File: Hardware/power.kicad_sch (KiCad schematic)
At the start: 29 parts, among them IC1 LTC4413EDD#PBF, Q6 BUK9M11-40EX, Q8 DMP3099L, U3 LM66200DRLR, U4 MAX77827AEFD+T, U5 SC4215ASTRT

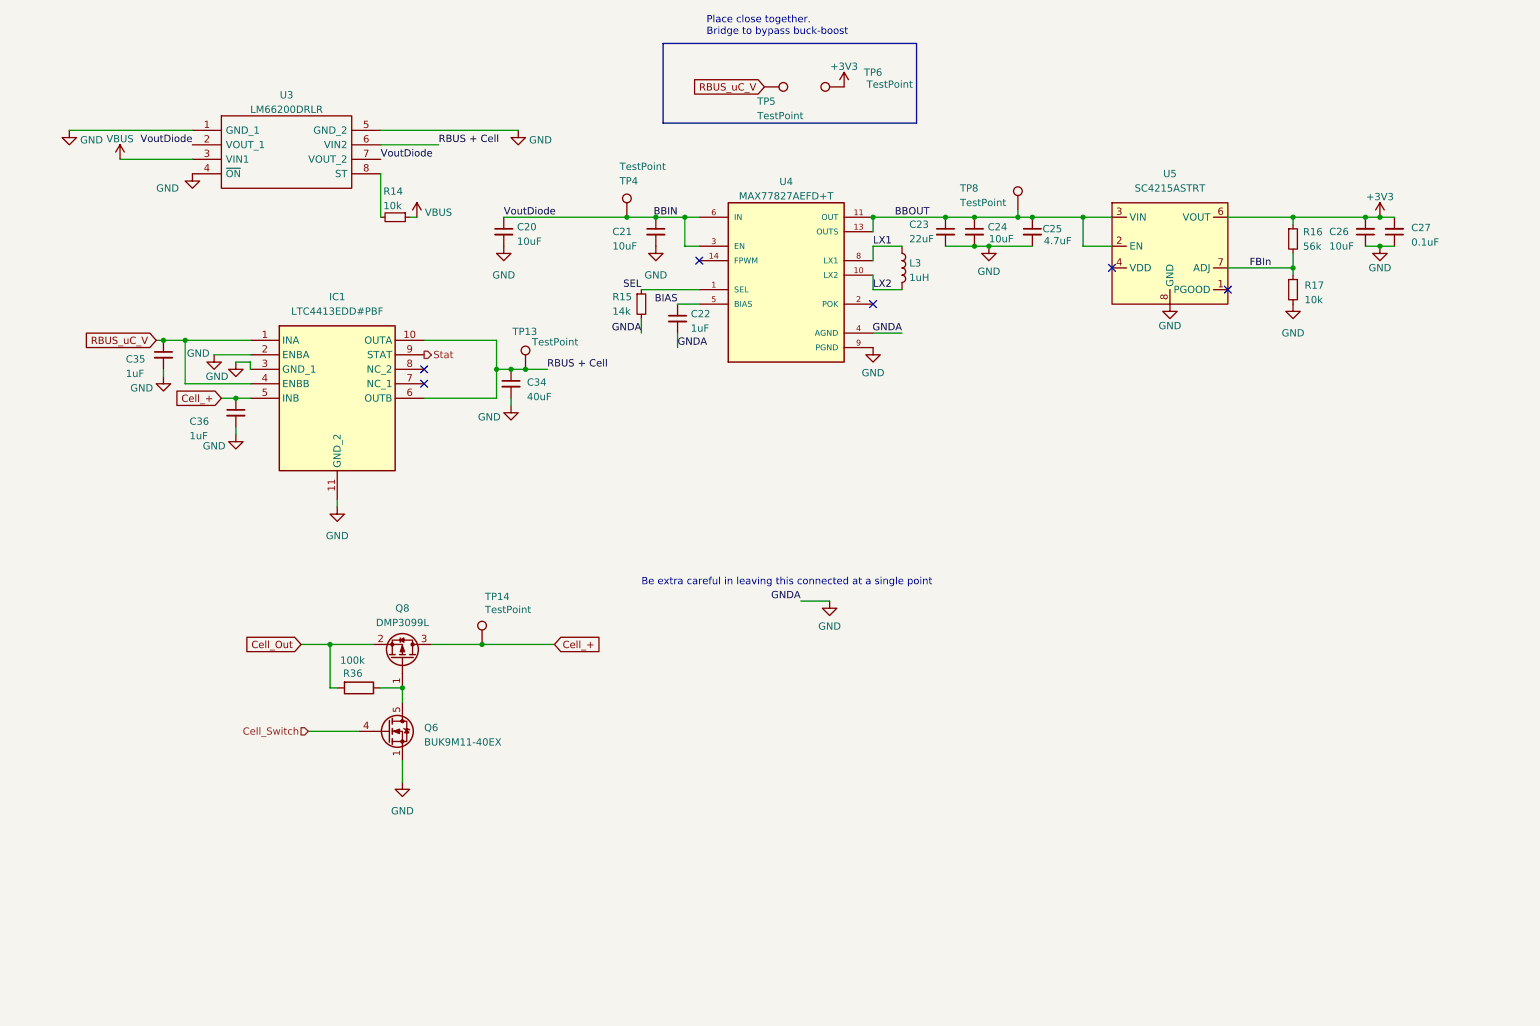
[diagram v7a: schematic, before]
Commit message: Crosshair post review 2
Layout redesign + changes implemented. Traces not yet complete
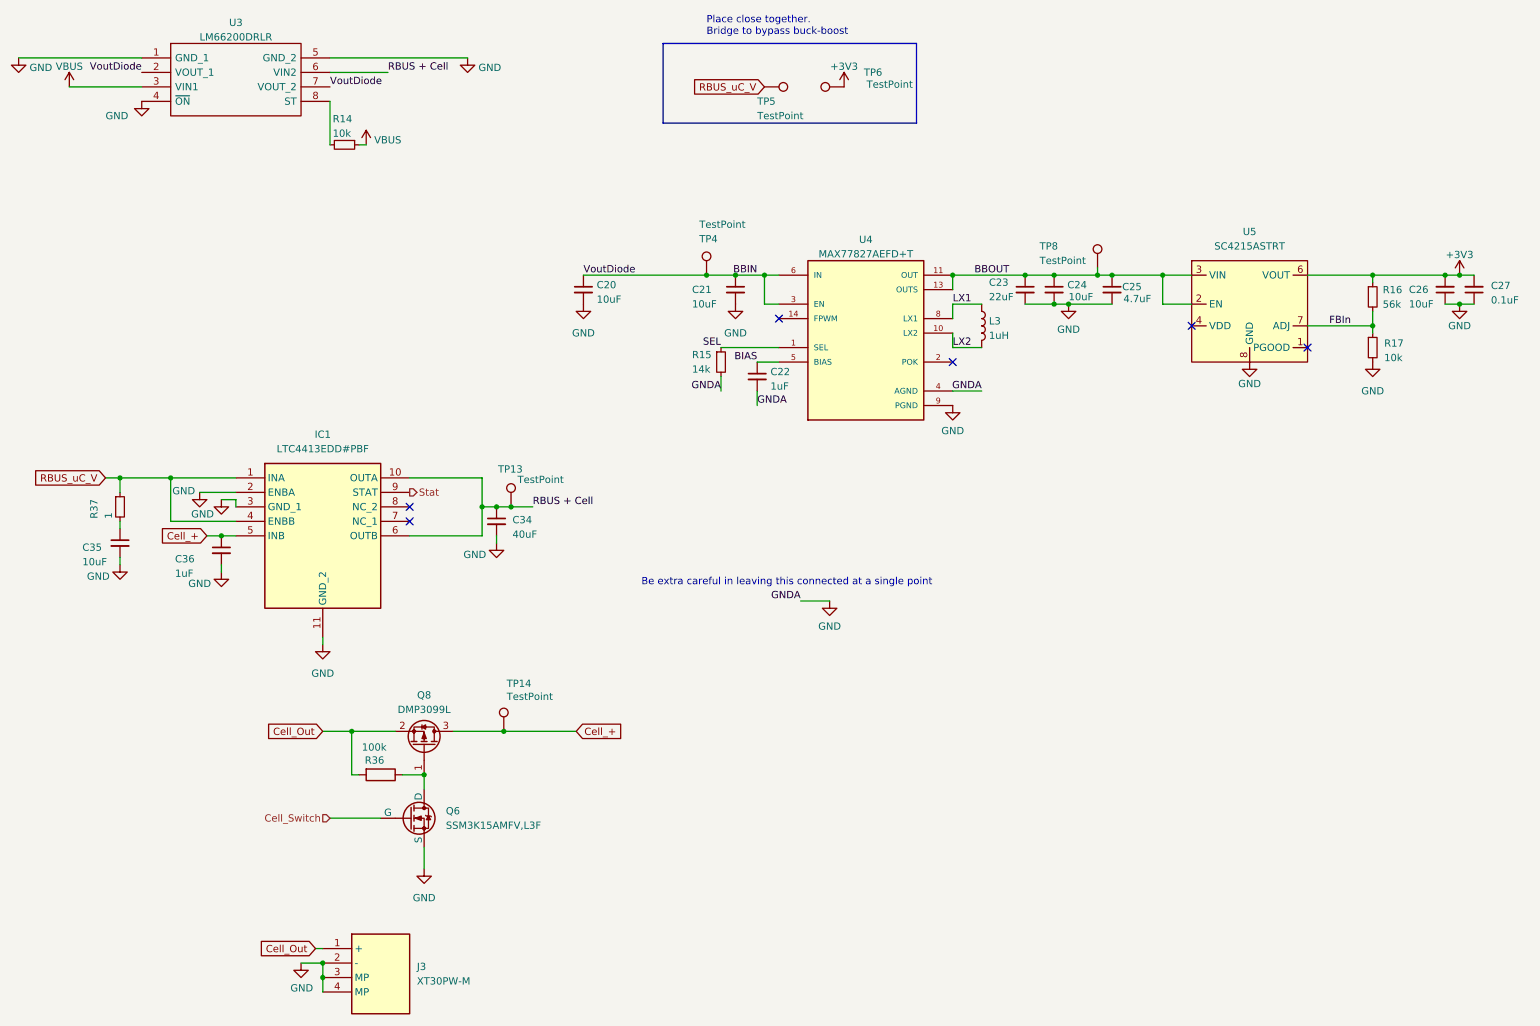
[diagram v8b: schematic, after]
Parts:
- removed Q6: BUK9M11-40EX, Package_TO_SOT_SMD:LFPAK33, symbol Transistor_FET:BUK9M11-40EX
- added J3: XT30PW-M, iclr:XT30PWM, symbol iclr:XT30PW-M
- added Q6: SSM3K15AMFV,L3F, iclr:SOT-723, symbol Simulation_SPICE:NMOS
- added R37: 1, Resistor_SMD:R_0402_1005Metric, symbol Device:R_Small
- C35: value 1uF -> 10uF
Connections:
- net Cell_Out: now also J3.1 (+)
- net Cell_Switch: now also Q6.2 (G)
- net GND: now also J3.2 (-), J3.3 (MP), J3.4 (MP), Q6.3 (S)
- net RBUS_uC_V: now also R37.1; no longer C35.1
- net at Q8.1 (G), R36.1: now also Q6.1 (D)
- new net: C35.1, R37.2
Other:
- moved on the sheet: C20, C21, C22, C23, C24, C25, C26, C27, C34, C35, C36, IC1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
